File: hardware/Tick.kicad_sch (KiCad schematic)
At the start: 39 parts, among them J1 Conn_01x03, J2 Conn_01x02, J3 Conn_01x04, J4 Conn_01x03, Q1 2N7002, Q2 2N7002, Q3 2N7002, Q4 2N7002, U1 LMR51430YDDCR, U2 THVD1400D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

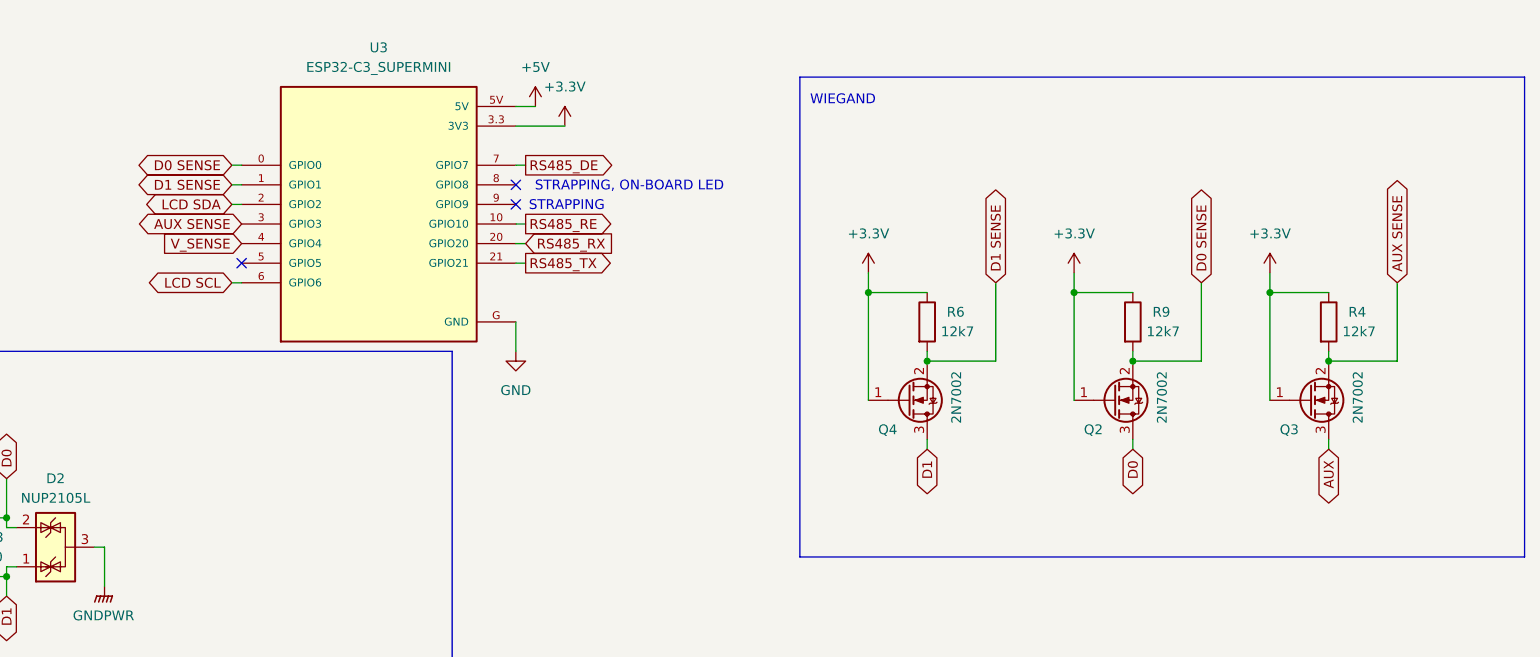
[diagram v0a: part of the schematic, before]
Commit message: added strong current sink on AUX
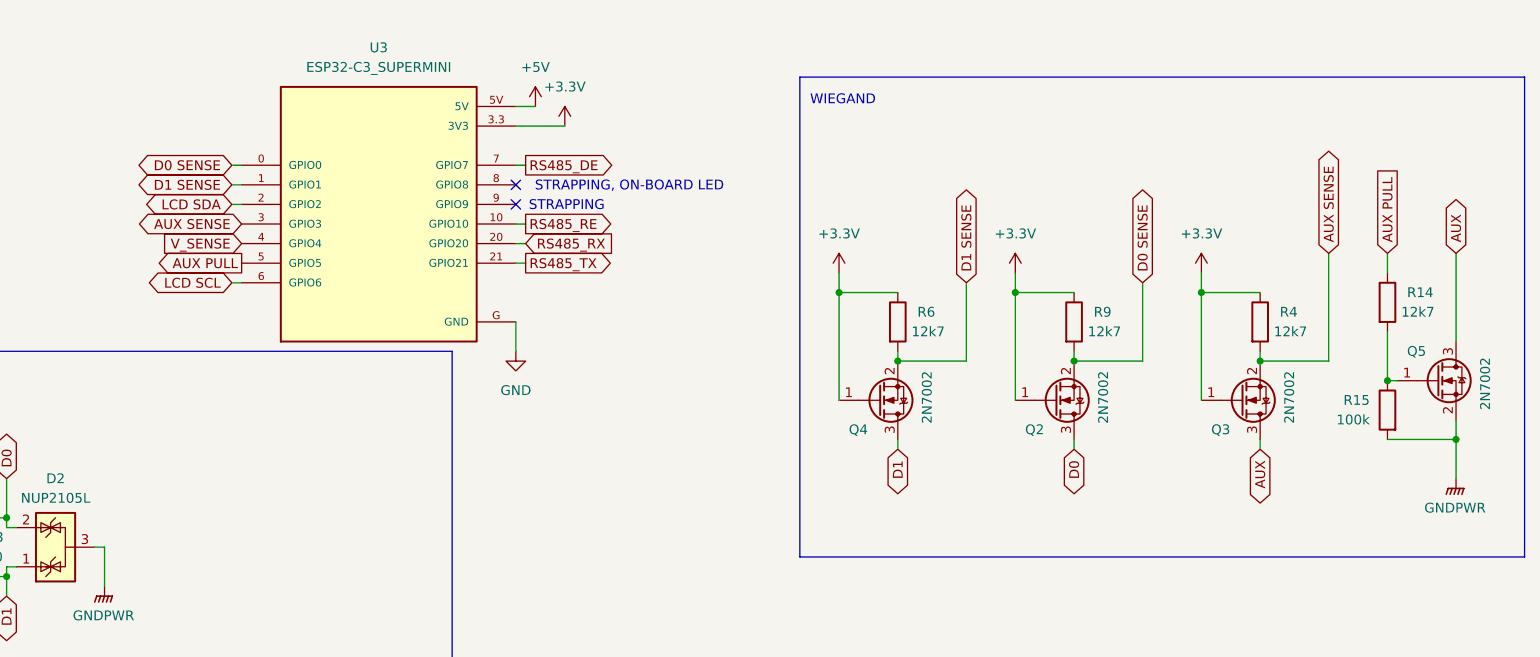
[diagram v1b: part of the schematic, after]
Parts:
- added Q5: 2N7002, Package_TO_SOT_SMD:SOT-23, symbol Transistor_FET:2N7002
- added R14: 12k7, Resistor_SMD:R_0603_1608Metric_Pad0.98x0.95mm_HandSolder, symbol Device:R
- added R15: 100k, Resistor_SMD:R_0603_1608Metric_Pad0.98x0.95mm_HandSolder, symbol Device:R
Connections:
- net AUX: now also Q5.3 (D)
- net GNDPWR: now also Q5.2 (S), R15.2
- net AUX PULL: now reaches U3.5 (GPIO5)
- net AUX PULL: now also R14.1
- new net: Q5.1 (G), R14.2, R15.1
- no-connect marks 4 -> 3
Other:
- moved on the sheet: Q2, Q3, Q4, R4, R6, R9
